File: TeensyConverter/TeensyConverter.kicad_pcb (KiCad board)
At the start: 2 copper layers, 5 parts, among them P101 CONN_01X03, U101 Teensy-3.2, U102 CE_Header

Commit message: Created the layout and submitted to OSH Park
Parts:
- removed P101: CONN_01X03, Pin_Headers:Pin_Header_Straight_1x03_Pitch2.54mm
- removed R101, R102: R, Resistors_SMD:R_0805_HandSoldering
- removed U101: Teensy-3.2, TeencyConverter:Teensy-32
- removed U102: CE_Header, TeencyConverter:CE_Header
- added H1: CE_Header, CE_Header:CE_Header, F.Cu at (102.4, 104.1)
- added P1: CONN_01X03, TeencyConverter:Pin_Header_Straight_1x03_Pitch2.54mm, F.Cu at (108.2, 98.8)
- added R1: R, Resistors_SMD:R_0805_HandSoldering, F.Cu at (110.5, 104.4)
- added R2: R, Resistors_SMD:R_0805_HandSoldering, F.Cu at (108.5, 104.4)
- added U1: Teensy-3.2, TeencyConverter:Teensy-32, B.Cu at (105.4, 113.0)
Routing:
- net /SPI_CLK: track 0.00 -> 42.1 mm
- net /SPI_MISO: track 0.00 -> 32.5 mm
- net /SPI_MOSI: track 0.00 -> 29.3 mm
- net /3V3: track 0.00 -> 23.9 mm
- net /SPI_CS: track 0.00 -> 23.7 mm
- net /DEVICE_RX: track 0.00 -> 17.5 mm
- net /5V: track 0.00 -> 13.0 mm
- net /AIO_0: track 0.00 -> 12.4 mm
- net /AIO_2: track 0.00 -> 10.9 mm
- net /AIO_1: track 0.00 -> 9.73 mm
- net /AIO_3: track 0.00 -> 8.69 mm
- net /I2C_DAT: track 0.00 -> 7.89 mm
- net /DEVICE_TX: track 0.00 -> 7.49 mm, vias 0 -> 1
- net /PWR_IO: track 0.00 -> 6.70 mm
- net /TEENCY_RX: track 0.00 -> 6.24 mm
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- added copper zone on B.Cu, net /GND
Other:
- board outline added: 20.3 x 38.1 mm
- net class Default: clearance 0.2 -> 0.1524; trace_width 0.25 -> 0.1524; via_dia 0.6 -> 0.6858; via_drill 0.4 -> 0.3302
- rule pad_to_mask_clearance: 0.2 -> 0.1524
- rule trace_clearance: 0.2 -> 0.1524
- rule trace_min: 0.2 -> 0.1524
- rule via_min_drill: 0.3 -> 0.3302
- rule via_min_size: 0.4 -> 0.6858
- board text added: "2L_1"
- board text added: "3V3"
- board text added: "5V"
- board text added: "A0"
- board text added: "A1"
- board text added: "A2"
- board text added: "A3"
- board text added: "CE Header"
- board text added: "CLK"
- board text added: "CS"
- board text added: "GND"
- board text added: "MISO"
- board text added: "MOSI"
- board text added: "PWR"
- board text added: "Rx"
- board text added: "SCK"
- board text added: "SDA"
- board text added: "Teensy"
- board text added: "Teensy Breakout"
- board text added: "Tx"

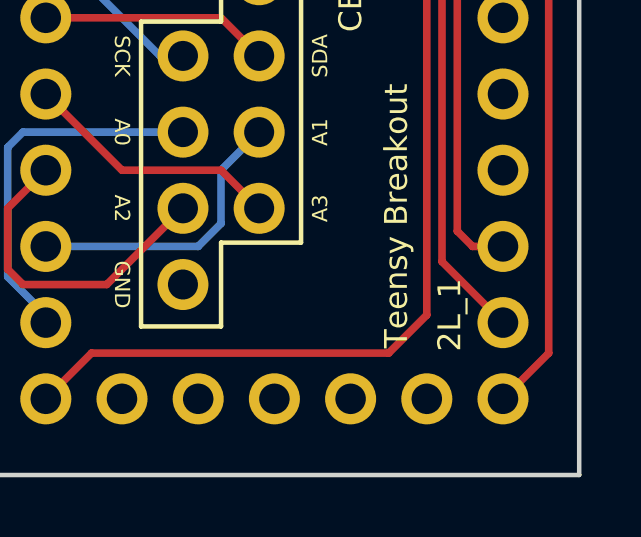
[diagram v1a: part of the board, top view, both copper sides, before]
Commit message: Corrected the soldermask spec
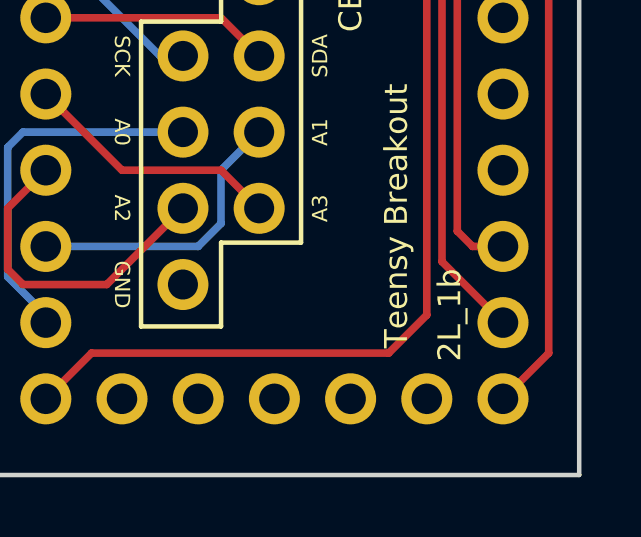
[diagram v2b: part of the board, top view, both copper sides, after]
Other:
- rule pad_to_mask_clearance: 0.1524 -> 0
- board text added: "2L_1b"
- board text removed: "2L_1"
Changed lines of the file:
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@@
     (pad_size 1.524 1.524)
     (pad_drill 0.762)
-    (pad_to_mask_clearance 0.1524)
+    (pad_to_mask_clearance 0)
     (aux_axis_origin 0 0)
     (visible_elements 7FFEEFFF)
     (pcbplotparams
-      (layerselection 0x000f0_80000001)
+      (layerselection 0x010f0_80000001)
       (usegerberextensions false)
       (excludeedgelayer true)
@@
       (drillshape 0)
       (scaleselection 1)
-      (outputdirectory ""))
+      (outputdirectory gerbers/))
   )
   (net 0 "")
@@
     (effects (font (size 0.508 0.508) (thickness 0.127)))
   )
-  (gr_text 2L_1 (at 111.252 128.016 90) (layer F.SilkS)
+  (gr_text 2L_1b (at 111.252 128.016 90) (layer F.SilkS)
     (effects (font (size 0.762 0.762) (thickness 0.127)))
   )

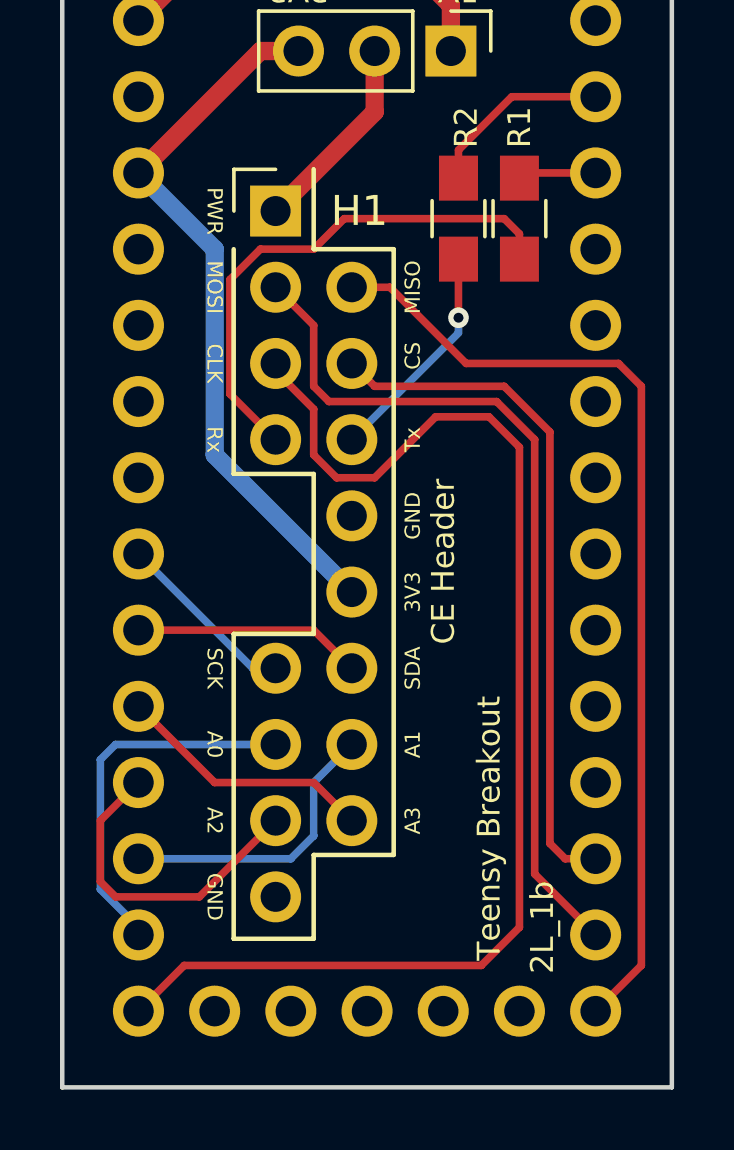
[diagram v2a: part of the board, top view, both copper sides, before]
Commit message: Correction to the teensy adapter for the pull ups
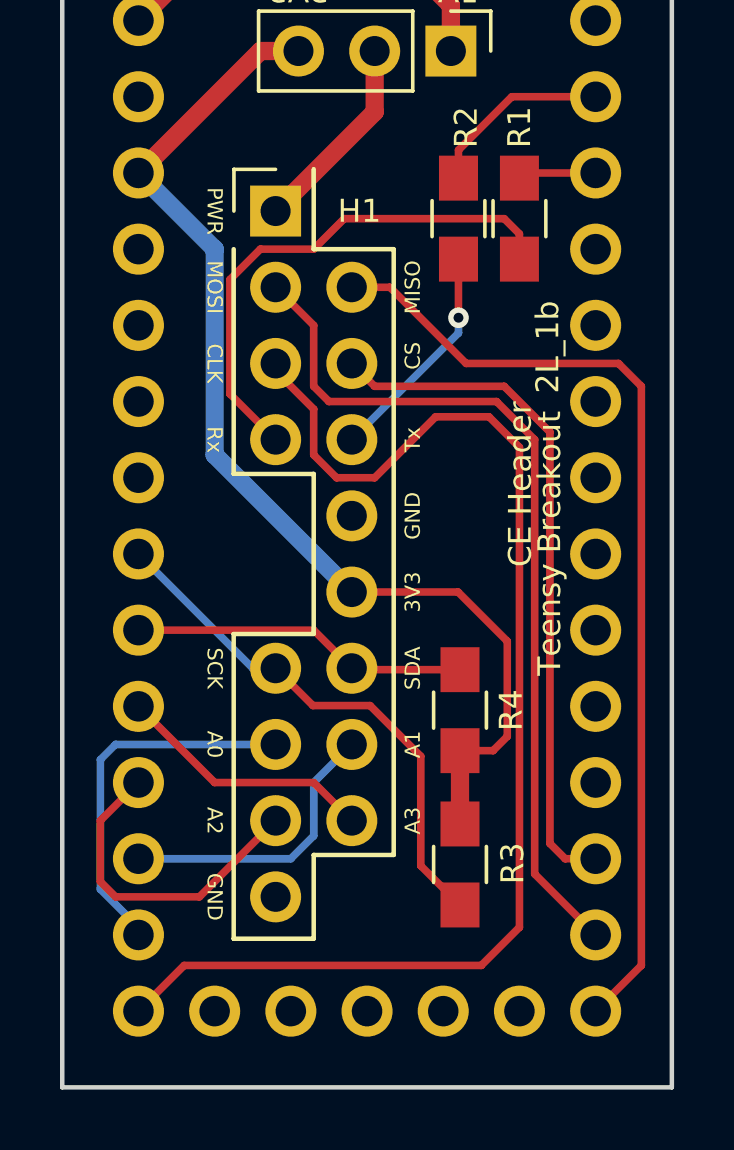
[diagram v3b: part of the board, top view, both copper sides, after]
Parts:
- added R3: 4.7kΩ, Resistors_SMD:R_0805_HandSoldering, F.Cu at (108.5, 125.9)
- added R4: 4.7kΩ, Resistors_SMD:R_0805_HandSoldering, F.Cu at (108.5, 120.8)
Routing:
- net /3V3: track 23.9 -> 37.2 mm
- net /I2C_SCLK: track 6.15 -> 17.7 mm
- net /I2C_DAT: track 7.89 -> 11.5 mm
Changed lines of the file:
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@@
 (kicad_pcb (version 4) (host pcbnew 4.0.0-rc1-stable)
   (general
-    (links 21)
+    (links 25)
     (no_connects 0)
-    (area 95.174999 94.3737 115.645001 133.425001)
+    (area 95.174999 95.174999 115.645001 133.425001)
     (thickness 1.6)
     (drawings 26)
-    (tracks 82)
+    (tracks 95)
     (zones 0)
-    (modules 5)
+    (modules 7)
     (nets 36)
   )
@@
   )
   (setup
-    (last_trace_width 0.1524)
+    (last_trace_width 0.254)
     (user_trace_width 0.254)
     (user_trace_width 0.3048)
@@
     (tags "CE Header, THT 2x10 2.54mm")
     (fp_text reference H1 (at 2.794 0) (layer F.SilkS)
-      (effects (font (size 1 1) (thickness 0.15)))
+      (effects (font (size 0.762 0.762) (thickness 0.127)))
     )
     (fp_text value CE_Header (at 1.27 25.25) (layer F.Fab)
-      (effects (font (size 1 1) (thickness 0.15)))
+      (effects (font (size 0.762 0.762) (thickness 0.127)))
     )
     (fp_line (start -1.397 24.257) (end -1.397 14.097) (layer F.SilkS) (width 0.15))
@@
     )
   )
-  (gr_text "Teensy Breakout" (at 109.474 124.714 90) (layer F.SilkS)
+  (module Resistors_SMD:R_0805_HandSoldering (layer F.Cu)
+    (at 108.5088 125.9205 90)
+    (descr "Resistor SMD 0805, hand soldering")
+    (tags "resistor 0805")
+    (attr smd)
+    (fp_text reference R3 (at 0.0381 1.7526 90) (layer F.SilkS)
+      (effects (font (size 0.762 0.762) (thickness 0.127)))
+    )
+    (fp_text value 4.7kΩ (at 0 1.75 90) (layer F.Fab)
+      (effects (font (size 0.762 0.762) (thickness 0.127)))
+    )
+    (fp_text user %R (at 0 0 90) (layer F.Fab)
+      (effects (font (size 0.762 0.762) (thickness 0.127)))
+    )
+    (fp_line (start -1 0.62) (end -1 -0.62) (layer F.Fab) (width 0.1))
+    (fp_line (start 1 0.62) (end -1 0.62) (layer F.Fab) (width 0.1))
+    (fp_line (start 1 -0.62) (end 1 0.62) (layer F.Fab) (width 0.1))
+    (fp_line (start -1 -0.62) (end 1 -0.62) (layer F.Fab) (width 0.1))
+    (fp_line (start 0.6 0.88) (end -0.6 0.88) (layer F.SilkS) (width 0.12))
+    (fp_line (start -0.6 -0.88) (end 0.6 -0.88) (layer F.SilkS) (width 0.12))
+    (fp_line (start -2.35 -0.9) (end 2.35 -0.9) (layer F.CrtYd) (width 0.05))
+    (fp_line (start -2.35 -0.9) (end -2.35 0.9) (layer F.CrtYd) (width 0.05))
+    (fp_line (start 2.35 0.9) (end 2.35 -0.9) (layer F.CrtYd) (width 0.05))
+    (fp_line (start 2.35 0.9) (end -2.35 0.9) (layer F.CrtYd) (width 0.05))
+    (pad 1 smd rect (at -1.35 0 90) (size 1.5 1.3) (layers F.Cu F.Paste F.Mask)
+      (net 17 /I2C_SCLK))
+    (pad 2 smd rect (at 1.35 0 90) (size 1.5 1.3) (layers F.Cu F.Paste F.Mask)
+      (net 3 /3V3))
+    (model ${KISYS3DMOD}/Resistors_SMD.3dshapes/R_0805.wrl
+      (at (xyz 0 0 0))
+      (scale (xyz 1 1 1))
+      (rotate (xyz 0 0 0))
+    )
+  )
+  (module Resistors_SMD:R_0805_HandSoldering (layer F.Cu)
+    (at 108.5088 120.777 270)
+    (descr "Resistor SMD 0805, hand soldering")
+    (tags "resistor 0805")
+    (attr smd)
+    (fp_text reference R4 (at 0 -1.7 270) (layer F.SilkS)
+      (effects (font (size 0.762 0.762) (thickness 0.127)))
+    )
+    (fp_text value 4.7kΩ (at 0 1.75 270) (layer F.Fab)
+      (effects (font (size 0.762 0.762) (thickness 0.127)))
+    )
+    (fp_text user %R (at 0 0 270) (layer F.Fab)
+      (effects (font (size 0.762 0.762) (thickness 0.127)))
+    )
+    (fp_line (start -1 0.62) (end -1 -0.62) (layer F.Fab) (width 0.1))
+    (fp_line (start 1 0.62) (end -1 0.62) (layer F.Fab) (width 0.1))
+    (fp_line (start 1 -0.62) (end 1 0.62) (layer F.Fab) (width 0.1))
+    (fp_line (start -1 -0.62) (end 1 -0.62) (layer F.Fab) (width 0.1))
+    (fp_line (start 0.6 0.88) (end -0.6 0.88) (layer F.SilkS) (width 0.12))
+    (fp_line (start -0.6 -0.88) (end 0.6 -0.88) (layer F.SilkS) (width 0.12))
+    (fp_line (start -2.35 -0.9) (end 2.35 -0.9) (layer F.CrtYd) (width 0.05))
+    (fp_line (start -2.35 -0.9) (end -2.35 0.9) (layer F.CrtYd) (width 0.05))
+    (fp_line (start 2.35 0.9) (end 2.35 -0.9) (layer F.CrtYd) (width 0.05))
+    (fp_line (start 2.35 0.9) (end -2.35 0.9) (layer F.CrtYd) (width 0.05))
+    (pad 1 smd rect (at -1.35 0 270) (size 1.5 1.3) (layers F.Cu F.Paste F.Mask)
+      (net 16 /I2C_DAT))
+    (pad 2 smd rect (at 1.35 0 270) (size 1.5 1.3) (layers F.Cu F.Paste F.Mask)
+      (net 3 /3V3))
+    (model ${KISYS3DMOD}/Resistors_SMD.3dshapes/R_0805.wrl
+      (at (xyz 0 0 0))
+      (scale (xyz 1 1 1))
+      (rotate (xyz 0 0 0))
+    )
+  )
+  (gr_text "Teensy Breakout" (at 111.4933 115.2144 90) (layer F.SilkS)
     (effects (font (size 0.762 0.762) (thickness 0.127)))
   )
@@
     (effects (font (size 0.508 0.508) (thickness 0.127)))
   )
-  (gr_text 2L_1b (at 111.252 128.016 90) (layer F.SilkS)
+  (gr_text 2L_1b (at 111.4298 108.6739 90) (layer F.SilkS)
     (effects (font (size 0.762 0.762) (thickness 0.127)))
   )
-  (gr_text "CE Header" (at 107.95 115.824 90) (layer F.SilkS)
+  (gr_text "CE Header" (at 110.5154 113.2459 90) (layer F.SilkS)
     (effects (font (size 0.762 0.762) (thickness 0.127)))
   )
@@
   (segment (start 102.362 104.14) (end 105.664 100.838) (width 0.6096) (layer F.Cu) (net 2))
   (segment (start 105.664 100.838) (end 105.664 98.806) (width 0.6096) (layer F.Cu) (net 2))
+  (segment (start 108.5088 122.127) (end 109.6099 122.127) (width 0.254) (layer F.Cu) (net 3))
+  (segment (start 108.4453 116.84) (end 104.902 116.84) (width 0.254) (layer F.Cu) (net 3))
+  (segment (start 110.083598 118.478298) (end 108.4453 116.84) (width 0.254) (layer F.Cu) (net 3))
+  (segment (start 110.083598 121.653302) (end 110.083598 118.478298) (width 0.254) (layer F.Cu) (net 3))
+  (segment (start 109.6099 122.127) (end 110.083598 121.653302) (width 0.254) (layer F.Cu) (net 3))
+  (segment (start 108.5088 124.5705) (end 108.5088 122.127) (width 0.6096) (layer F.Cu) (net 3))
   (segment (start 101.854 98.806) (end 103.124 98.806) (width 0.6096) (layer F.Cu) (net 3))
   (segment (start 100.33 112.268) (end 104.902 116.84) (width 0.6096) (layer B.Cu) (net 3))
+  (segment (start 97.79 102.87) (end 100.33 105.41) (width 0.6096) (layer B.Cu) (net 3))
   (segment (start 100.33 105.41) (end 100.33 112.268) (width 0.6096) (layer B.Cu) (net 3))
   (segment (start 97.79 102.87) (end 101.854 98.806) (width 0.6096) (layer F.Cu) (net 3))
-  (segment (start 97.79 102.87) (end 100.33 105.41) (width 0.6096) (layer B.Cu) (net 3))
   (segment (start 110.49 105.744) (end 110.49 104.902) (width 0.254) (layer F.Cu) (net 4))
   (segment (start 100.838 110.236) (end 102.362 111.76) (width 0.254) (layer F.Cu) (net 4))
@@
   (segment (start 100.33 123.19) (end 103.632 123.19) (width 0.254) (layer F.Cu) (net 15))
   (segment (start 97.79 120.65) (end 100.33 123.19) (width 0.254) (layer F.Cu) (net 15))
+  (segment (start 108.5088 119.427) (end 104.949 119.427) (width 0.254) (layer F.Cu) (net 16))
+  (segment (start 104.949 119.427) (end 104.902 119.38) (width 0.254) (layer F.Cu) (net 16))
   (segment (start 97.79 118.11) (end 103.632 118.11) (width 0.254) (layer F.Cu) (net 16))
   (segment (start 103.632 118.11) (end 104.902 119.38) (width 0.254) (layer F.Cu) (net 16))
   (segment (start 97.79 118.11) (end 97.536 118.11) (width 0.254) (layer F.Cu) (net 16))
+  (segment (start 108.5088 127.2705) (end 107.2007 125.9624) (width 0.254) (layer F.Cu) (net 17) (status 400000))
+  (segment (start 103.6066 120.6246) (end 102.362 119.38) (width 0.254) (layer F.Cu) (net 17) (status 800000))
+  (segment (start 105.5116 120.6246) (end 103.6066 120.6246) (width 0.254) (layer F.Cu) (net 17))
+  (segment (start 107.2007 122.3137) (end 105.5116 120.6246) (width 0.254) (layer F.Cu) (net 17))
+  (segment (start 107.2007 125.9624) (end 107.2007 122.3137) (width 0.254) (layer F.Cu) (net 17))
   (segment (start 97.79 115.57) (end 101.6 119.38) (width 0.254) (layer B.Cu) (net 17))
   (segment (start 101.6 119.38) (end 102.362 119.38) (width 0.254) (layer B.Cu) (net 17))
